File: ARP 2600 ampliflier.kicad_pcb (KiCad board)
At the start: 2 copper layers, 100 x 100 mm, 32 parts, among them P1 CONN_01X04, P2 CONN_01X04, P3 CONN_01X04, P4 CONN_01X04, U1 TDA7269A, U2 LM7812CT, U3 LM7912CT

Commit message: routed
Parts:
- P1, P2, P3, P4: footprint Connectors_Terminal_Blocks:TerminalBlock_Pheonix_MPT-2.54mm_4pol -> w_conn_mpt:mpt_0,5%2f4-2,54
- U1: footprint w_to:Multiwatt11 -> MyModules:Multiwatt11-6400BG
- moved P3 92.9 mm to (99.0, 114.0), turned to 270 degrees
- moved U3 81.5 mm to (119.0, 133.0), turned to 270 degrees
- moved D4 63.4 mm to (111.0, 112.0), turned to 270 degrees
- moved P4 60.3 mm to (151.0, 75.0), turned to 180 degrees
- moved D3 52.9 mm to (111.0, 99.0), turned to 270 degrees
- moved D1 51.4 mm to (107.0, 99.0), turned to 270 degrees
- moved C4 50.1 mm to (158.0, 86.0), turned to 270 degrees
- moved P1 47.8 mm to (145.0, 144.0)
- moved C2 47.7 mm to (154.0, 144.0), turned to 180 degrees
- moved C1 46.6 mm to (136.0, 144.0)
- moved U1 46.1 mm to (147.0, 117.0), turned to 270 degrees
- moved C5 42.6 mm to (178.0, 128.0), turned to 90 degrees
- moved C6 42.3 mm to (177.0, 102.0), turned to 270 degrees
- moved R6 40.0 mm to (178.0, 132.0), turned to 180 degrees
- moved C3 38.7 mm to (144.0, 86.0), turned to 270 degrees
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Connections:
- U1 pad 8: (no net) -> Net-(R2-Pad2)
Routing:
- net -V: track 0.00 -> 81.0 mm
- net +V: track 0.00 -> 69.7 mm
- net Net-(P2-Pad1): track 0.00 -> 44.6 mm
- net Net-(C8-Pad2): track 0.00 -> 37.1 mm
- net Net-(P2-Pad4): track 0.00 -> 34.6 mm
- net Net-(C7-Pad1): track 0.00 -> 31.5 mm
- net Net-(C1-Pad1): track 0.00 -> 29.4 mm
- net Net-(R2-Pad2): track 0.00 -> 28.5 mm
- net Net-(R4-Pad1): track 0.00 -> 28.0 mm
- net Net-(C2-Pad1): track 0.00 -> 23.9 mm
- net Net-(D3-Pad2): track 0.00 -> 18.3 mm
- net Net-(D1-Pad2): track 0.00 -> 11.6 mm
- net Net-(R1-Pad1): track 0.00 -> 10.1 mm
- net Net-(C5-Pad1): track 0.00 -> 6.76 mm
- net Net-(C6-Pad1): track 0.00 -> 4.48 mm
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- added copper zone on B.Cu, net GND
- added copper zone on F.Cu, net GND
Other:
- board size 100 x 100 mm -> 88 x 81 mm
- net class Default: clearance 0.2 -> 0.25; trace_width 0.25 -> 0.35; via_dia 0.6 -> 0.8; via_drill 0.4 -> 0.5
- net class Power added: clearance 0.25, trace_width 0.65, via_dia 0.8, via_drill 0.5
- rule trace_clearance: 0.2 -> 0.25

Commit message: few tweaks, exported .png of 3D view
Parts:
- added HOLE-0.125-INCH: VAL**, MyModules:HOLE-0.125-INCH, F.Cu at (176.0, 77.0)
- added HOLE-0.125-INCH: VAL**, MyModules:HOLE-0.125-INCH, F.Cu at (176.0, 146.0)
- added HOLE-0.125-INCH: VAL**, MyModules:HOLE-0.125-INCH, F.Cu at (100.0, 77.0)
- added HOLE-0.125-INCH: VAL**, MyModules:HOLE-0.125-INCH, F.Cu at (100.0, 146.0)
- added REF***: OSHW-Symbol_8.9x8mm_SilkScreen, Symbols:OSHW-Symbol_8.9x8mm_SilkScreen, F.Cu at (165.2, 142.8)
- moved R3 1.80 mm to (170.5, 111.0)
- moved R5 1.60 mm to (170.8, 115.0)
- moved R2 1.41 mm to (167.0, 101.0)
- moved R4 1.41 mm to (167.0, 125.0)
- moved R7 1.35 mm to (166.8, 97.5)
- moved C5 1.00 mm to (178.0, 129.0)
- moved C6 1.00 mm to (177.0, 101.0)
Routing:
- net Net-(C5-Pad1): track 6.76 -> 8.84 mm
- net Net-(P2-Pad1): track 44.6 -> 46.1 mm
- net Net-(R2-Pad2): track 28.5 -> 27.4 mm
- net Net-(C6-Pad1): track 4.48 -> 3.57 mm
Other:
- board text added: "4Ω/8Ω"
- board text added: "AC"
- board text added: "COM"
- board text added: "IN(L)"
- board text added: "IN(R)"
- board text added: "OUT(L)"
- board text added: "OUT(R)"
- board text added: "P1-P4"
- board text added: "STEREO AUDIO AMPLIFIER"
- board text added: "V+"
- board text added: "V-"
- board text added: "system79.com"
- board text added: "v1.0 12 2016"

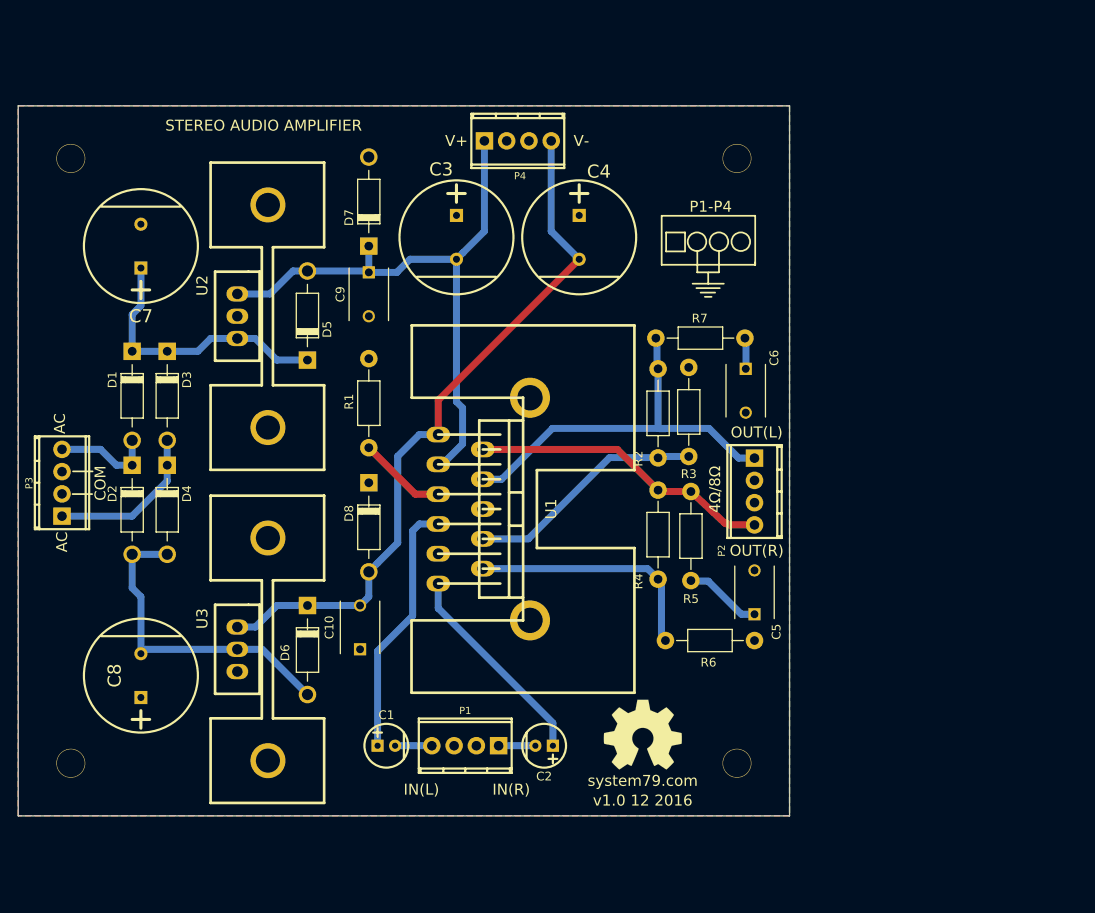
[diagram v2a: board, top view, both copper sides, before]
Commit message: added standby/mute control during power up, generated gerbers
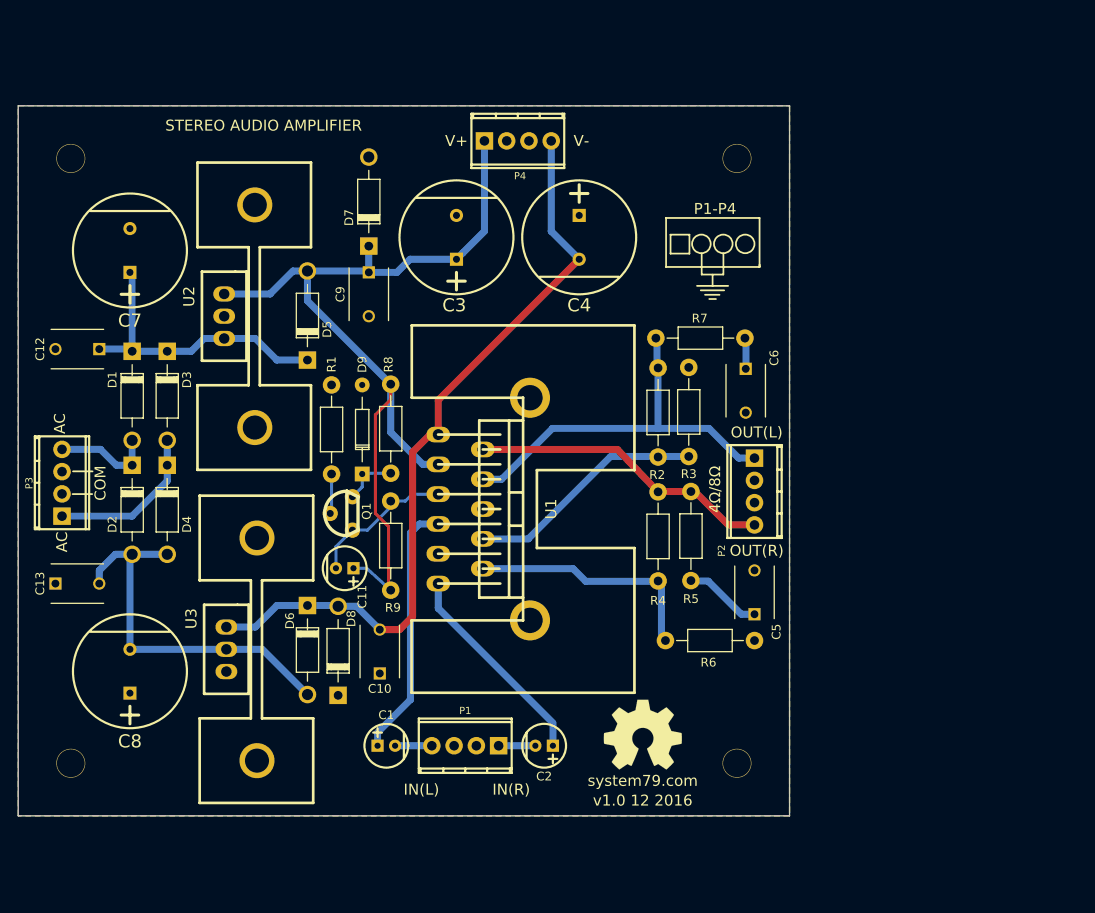
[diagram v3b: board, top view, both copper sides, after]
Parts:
- added C11: 1µ, MyModules:2MM-POL-CAP, F.Cu at (131.2, 123.8)
- added C12: 100n, Capacitors_THT:C_Disc_D6_P5, F.Cu at (103.2, 98.8)
- added C13: 100n, Capacitors_THT:C_Disc_D6_P5, F.Cu at (98.2, 125.5)
- added D9: 1N5231, Diodes_THT:Diode_DO-35_SOD27_Horizontal_RM10, F.Cu at (133.2, 113.0)
- added Q1: PN2222A, w_to:to92_3, F.Cu at (131.5, 117.5)
- added R8: 10K, Resistors_THT:Resistor_Horizontal_RM10mm, F.Cu at (136.5, 102.8)
- added R9: 10K, Resistors_THT:Resistor_Horizontal_RM10mm, F.Cu at (136.5, 126.2)
- R1: value 18K -> 10K
- moved D8 24.5 mm to (130.5, 138.2), turned to 90 degrees
- moved R1 5.20 mm to (129.8, 113.0)
- moved C10 3.55 mm to (135.2, 135.8)
- moved U2 1.50 mm to (117.5, 95.0)
- moved C7 1.35 mm to (106.8, 87.5)
- moved C8 1.35 mm to (106.8, 135.5)
- moved U3 1.25 mm to (117.8, 133.0)
- moved R4 0.20 mm to (167.0, 125.2)
- moved R2 0.10 mm to (167.0, 100.9)
- turned C3 to 90 degrees
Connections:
- C3 pad 1: GND -> +V
- C3 pad 2: +V -> GND
- R1 pad 1: Net-(R1-Pad1) -> Net-(Q1-Pad2)
- U1 pad 5: Net-(R1-Pad1) -> Net-(C11-Pad2)
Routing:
- net +V: track 69.7 -> 106.0 mm
- net Net-(C11-Pad2): track 0.00 -> 17.0 mm
- net Net-(R1-Pad1): track 10.1 -> 0.00 mm
- net -V: track 81.0 -> 88.0 mm
- net Net-(D9-Pad1): track 0.00 -> 6.35 mm
- net Net-(C13-Pad2): track 37.1 -> 43.3 mm
- net Net-(Q1-Pad2): track 0.00 -> 4.56 mm
- net Net-(C12-Pad1): track 31.5 -> 34.6 mm
- net Net-(P2-Pad1): track 46.1 -> 45.2 mm
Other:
- rule pad_to_mask_clearance: 0.2 -> 0.02

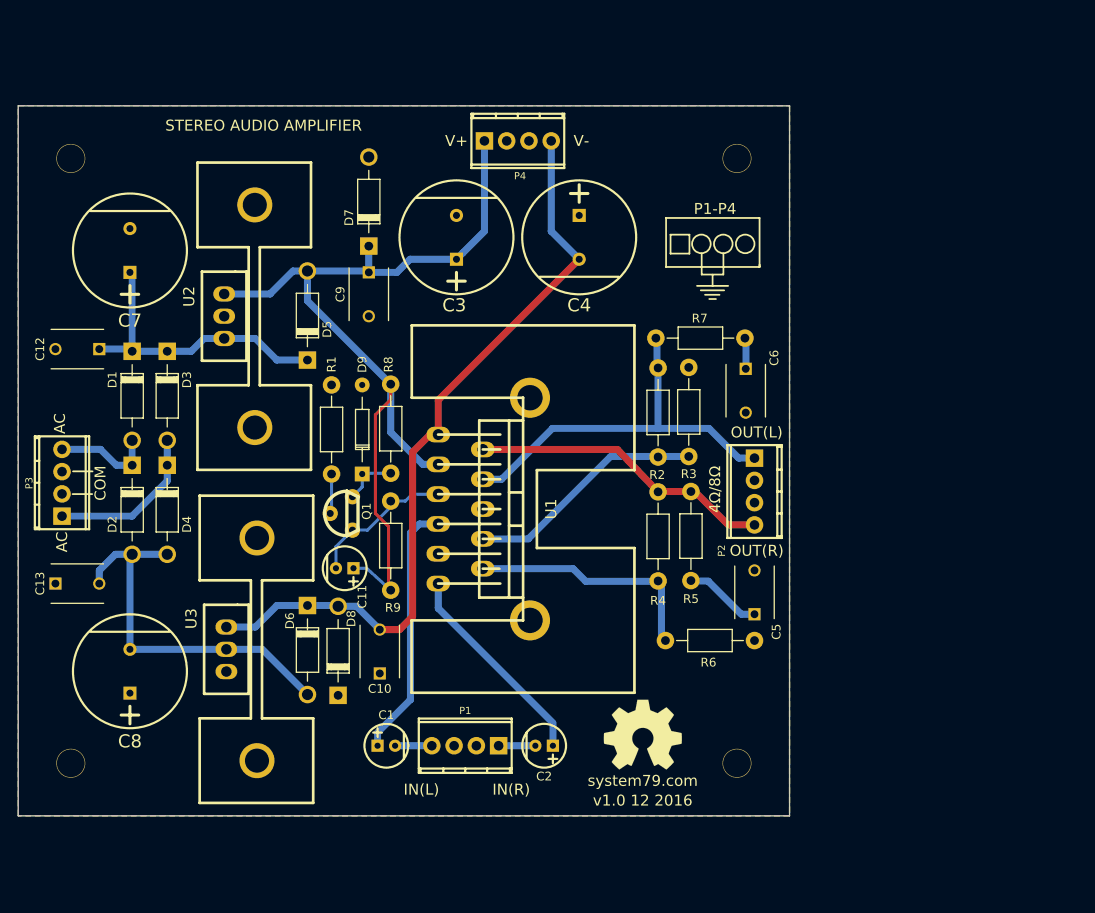
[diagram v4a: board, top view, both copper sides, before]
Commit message: fixed pintout error with T0-220 footprints, fix Q1 footprint pintout error, add keepout zones to heatsink landing areas on top copper
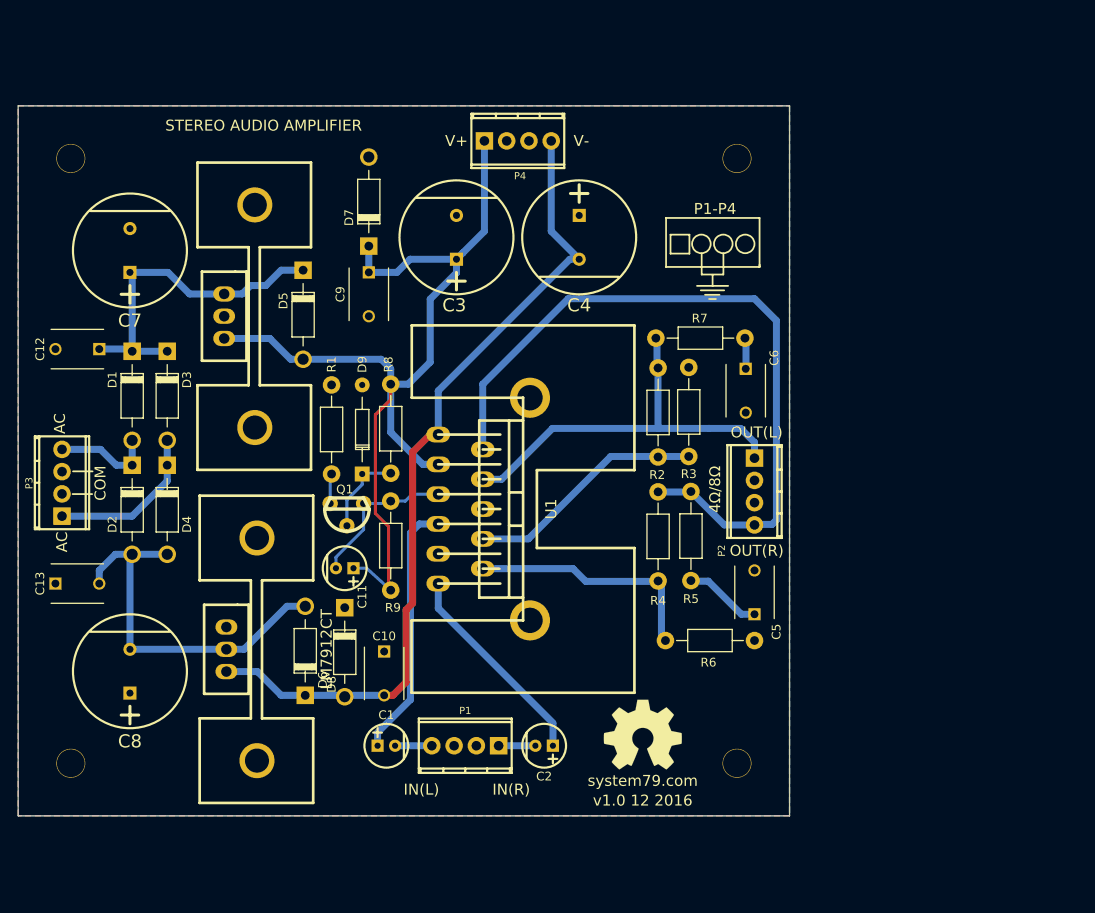
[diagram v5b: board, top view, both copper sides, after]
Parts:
- Q1: value PN2222A -> 2N3904
- U2, U3: footprint w_to:to220_std_11cw -> MyModules:TO220_HS346
- moved D5 10.3 mm to (126.5, 89.8), turned to 270 degrees
- moved D6 10.3 mm to (126.8, 138.2), turned to 90 degrees
- moved D8 10.0 mm to (131.2, 128.2), turned to 270 degrees
- moved C10 2.55 mm to (135.8, 133.2), turned to 270 degrees
- moved Q1 0.50 mm to (131.5, 117.0), turned to 180 degrees
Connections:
- Q1 pad 1: Net-(D9-Pad1) -> Net-(Q1-Pad1)
- Q1 pad 2: Net-(Q1-Pad2) -> Net-(D9-Pad1)
- R1 pad 1: Net-(Q1-Pad2) -> Net-(Q1-Pad1)
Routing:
- net Net-(P2-Pad4): track 34.7 -> 84.6 mm
- net -V: track 88.0 -> 94.8 mm
- net +V: track 106.0 -> 112.4 mm
- net Net-(Q1-Pad2): track 4.56 -> 0.00 mm
- net Net-(C12-Pad1): track 34.6 -> 38.9 mm
- net Net-(D9-Pad1): track 6.35 -> 9.92 mm
- net Net-(Q1-Pad1): track 0.00 -> 3.43 mm
- net Net-(C11-Pad2): track 17.0 -> 18.3 mm
- net Net-(P2-Pad1): track 45.2 -> 46.3 mm
